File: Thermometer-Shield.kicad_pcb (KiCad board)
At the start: 2 copper layers, 31 parts, among them J1 CONN_01X04, J2 CONN_01X02, J3 CONN_01X02, J4 CONN_01X02, J5 CONN_01X02, SW1 SW_SPST, SW2 SW_SPST, SW3 SW_SPST, SW4 SW_SPST, U1 ULN2803A

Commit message: schematic nearly done. PCB started
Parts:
- removed R0: 330, Resistors_SMD:R_0805_HandSoldering
- added J11: ShiftOut, Pin_Headers:Pin_Header_Straight_1x02_Pitch2.54mm, F.Cu at (171.4, 61.0)
- added J6: Out-D, Connectors:AK300-2, F.Cu at (181.6, 92.7)
- added J7: Out-E, Connectors:AK300-2, F.Cu at (191.8, 92.7)
- added J8: Out-F, Connectors:AK300-2, F.Cu at (201.9, 92.7)
- added JP1: CONN_02X02, Pin_Headers:Pin_Header_Straight_2x02_Pitch2.54mm, F.Cu at (190.5, 61.0)
- added O-A2: out, Connectors:1pin, F.Cu at (151.8, 125.7)
- added O-B2: out, Connectors:1pin, F.Cu at (165.7, 156.2)
- added Q1: Q_PNP_BCE, TO_SOT_Packages_THT:TO-92_Inline_Narrow_Oval, F.Cu at (154.9, 111.8)
- added Q2: Q_PNP_BCE, TO_SOT_Packages_THT:TO-92_Inline_Narrow_Oval, F.Cu at (148.6, 111.8)
- added Q3: Q_PNP_BCE, TO_SOT_Packages_THT:TO-92_Inline_Narrow_Oval, F.Cu at (155.6, 117.5)
- added Q4: Q_PNP_BCE, TO_SOT_Packages_THT:TO-92_Inline_Narrow_Oval, F.Cu at (149.9, 117.5)
- added R19: R, Resistors_SMD:R_0805_HandSoldering, B.Cu at (166.4, 74.9)
- added R20: R, Resistors_SMD:R_0805_HandSoldering, B.Cu at (172.1, 74.9)
- added R21: R, Resistors_SMD:R_0805_HandSoldering, B.Cu at (177.8, 74.3)
- added R22: R, Resistors_SMD:R_0805_HandSoldering, B.Cu at (184.2, 73.7)
- added U2: 74HC595, Housings_SSOP:TSSOP-16_4.4x5mm_Pitch0.65mm, B.Cu at (165.7, 62.9)
- added U3: ULN2803A, Housings_SOIC:SOIC-18W_7.5x11.6mm_Pitch1.27mm, B.Cu at (188.0, 81.3)
- J1: value CONN_01X04 -> Analog/I2C; footprint Pin_Headers:Pin_Header_Straight_1x04_Pitch2.54mm -> Pin_Headers:Pin_Header_Straight_1x06_Pitch2.54mm
- J2: value CONN_01X02 -> TempSensor; footprint Connectors:AK300-2 -> Pin_Headers:Pin_Header_Straight_1x04_Pitch2.54mm
- J3: value CONN_01X02 -> Out-A
- J4: value CONN_01X02 -> Out-B
- J5: value CONN_01X02 -> Out-C
- R1: value 330 -> A1050; footprint Resistors_SMD:R_0805_HandSoldering -> Opto-Devices:Resistor_LDR_D6.4_RM3.4; moved to F.Cu
- R10, R11, R12, R9: value 2K2 -> 330; footprint Resistors_SMD:R_0805_HandSoldering -> Resistors_SMD:R_0603_HandSoldering
- R15: value A1050 -> 2K2; footprint Opto-Devices:Resistor_LDR_D6.4_RM3.4 -> Resistors_SMD:R_0805_HandSoldering; moved to B.Cu
- R16, R17, R2: value 330 -> 2K2
- R3, R4, R5, R6, R7, R8: footprint Resistors_SMD:R_0805_HandSoldering -> Resistors_SMD:R_0603_HandSoldering
- U1: value ULN2803A -> 74HC595; footprint Housings_SOIC:SOIC-18W_7.5x11.6mm_Pitch1.27mm -> Housings_SSOP:TSSOP-16_4.4x5mm_Pitch0.65mm
- moved J1 107.9 mm to (222.9, 80.0), turned to 0 degrees
- moved R2 72.5 mm to (198.1, 100.3), turned to 180 degrees
- moved R4 65.3 mm to (144.8, 85.7)
- moved R1 64.8 mm to (212.1, 85.1)
- moved R5 60.5 mm to (144.8, 82.5)
- moved R12 60.4 mm to (144.8, 60.3), turned to 0 degrees
- moved R6 56.1 mm to (144.8, 79.4)
- moved R11 55.7 mm to (144.8, 63.5), turned to 0 degrees
- moved J2 52.2 mm to (201.3, 74.3), turned to 90 degrees
- moved Disp1 52.0 mm to (123.8, 64.1)
- moved R7 52.0 mm to (144.8, 76.2)
- moved R8 48.5 mm to (144.8, 73.0)
- moved R3 47.8 mm to (144.8, 54.6)
- moved R17 45.6 mm to (217.8, 109.2)
- moved R10 45.1 mm to (144.8, 66.7), turned to 0 degrees
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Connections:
- Disp1 pad 10: Net-(Disp1-Pad10) -> Dig2
- Disp1 pad 11: F -> Net-(Disp1-Pad11)
- Disp1 pad 13: C -> Net-(Disp1-Pad13)
- Disp1 pad 14: A -> Net-(Disp1-Pad14)
- Disp1 pad 15: G -> Net-(Disp1-Pad15)
- Disp1 pad 16: B -> Net-(Disp1-Pad16)
- Disp1 pad 3: D -> Net-(Disp1-Pad3)
- Disp1 pad 4: Extras -> Dig1
- Disp1 pad 5: E -> Net-(Disp1-Pad5)
- Disp1 pad 7: DP -> Net-(Disp1-Pad7)
- Disp1 pad 9: Extras -> Net-(Disp1-Pad9)
- J1 pad 1: +5V -> GND
- J1 pad 2: Temp-Data -> +5V
- J1 pad 3: (no net) -> Net-(J1-Pad3)
- J1 pad 4: GND -> Net-(J1-Pad4)
- J2 pad 1: /Out-A -> +5V
- J2 pad 2: GND -> Temp-Data
- J3 pad 1: /Out-B -> /Out-A
- J3 pad 2: GND -> VCC
- J4 pad 1: /Out-C -> /Out-B
- J4 pad 2: GND -> VCC
- J5 pad 1: /Out-D -> /Out-C
- J5 pad 2: GND -> VCC
- R1 pad 1: DP -> +5V
- R1 pad 2: Net-(R1-Pad2) -> Light
- R10 pad 1: Net-(R10-Pad1) -> Net-(Disp1-Pad7)
- R10 pad 2: Net-(R10-Pad2) -> DP
- R11 pad 1: Net-(R10-Pad2) -> Colon
- R11 pad 2: Net-(R11-Pad2) -> Net-(Disp1-Pad9)
- R12 pad 1: Net-(R11-Pad2) -> Degree
- R12 pad 2: Net-(R12-Pad2) -> Net-(Disp1-Pad12)
- R13 pad 1: Net-(R12-Pad2) -> +5V
- R13 pad 2: Buttons -> Net-(R13-Pad2)
- R14 pad 1: Buttons -> Net-(R13-Pad2)
- R14 pad 2: GND -> Net-(R14-Pad2)
- R15 pad 1: +5V -> Net-(R14-Pad2)
- R15 pad 2: Light -> Net-(R15-Pad2)
- R16 pad 1: Net-(Disp1-Pad10) -> Net-(R15-Pad2)
- R16 pad 2: +5V -> Net-(R16-Pad2)
- R17 pad 1: Net-(Disp1-Pad12) -> Net-(R16-Pad2)
- R17 pad 2: GND -> Buttons
- R18 pad 1: Light -> Buttons
- R2 pad 1: C -> Light
- R2 pad 2: Net-(R2-Pad2) -> GND
- R3 pad 1: B -> Net-(Disp1-Pad14)
- R3 pad 2: Net-(R3-Pad2) -> A
- R4 pad 1: A -> Net-(Disp1-Pad16)
- R4 pad 2: Net-(R4-Pad2) -> B
- R5 pad 1: F -> Net-(Disp1-Pad13)
- R5 pad 2: Net-(R5-Pad2) -> C
- R6 pad 1: G -> Net-(Disp1-Pad3)
- R6 pad 2: Net-(R6-Pad2) -> D
- R7 pad 1: D -> Net-(Disp1-Pad5)
- R7 pad 2: Net-(R7-Pad2) -> E
- R8 pad 1: E -> Net-(Disp1-Pad11)
- R8 pad 2: Net-(R8-Pad2) -> F
- R9 pad 1: +5V -> Net-(Disp1-Pad15)
- R9 pad 2: Net-(R10-Pad1) -> G
- SHIELD1 pad 0: Net-(R0-Pad2) -> (no net)
- SHIELD1 pad 1: Net-(R1-Pad2) -> (no net)
- SHIELD1 pad 10: Dig2 -> SS
- SHIELD1 pad 11: Dig3 -> MOSI
- SHIELD1 pad 12: Dig4 -> Net-(JP1-Pad1)
- SHIELD1 pad 13: Temp-Data -> SCK
- SHIELD1 pad 2: Net-(R2-Pad2) -> Temp-Data
- SHIELD1 pad 3: Net-(R3-Pad2) -> Trig-F
- SHIELD1 pad 4: Net-(R4-Pad2) -> Trig-E
- SHIELD1 pad 5: Net-(R5-Pad2) -> Trig-D
- SHIELD1 pad 6: Net-(R6-Pad2) -> Trig-C
- SHIELD1 pad 7: Net-(R7-Pad2) -> Trig-B
- SHIELD1 pad 8: Net-(R8-Pad2) -> Trig-A
- SHIELD1 pad 9: Dig1 -> Net-(JP1-Pad3)
- SHIELD1 pad AD2: Trig-D -> Net-(J1-Pad6)
- SHIELD1 pad AD3: Trig-C -> Net-(J1-Pad5)
- SHIELD1 pad AD4: Trig-B -> Net-(J1-Pad3)
- SHIELD1 pad AD5: Trig-A -> Net-(J1-Pad4)
- SHIELD1 pad V_IN: (no net) -> VCC
- SW1 pad 2: Net-(R10-Pad1) -> Net-(R13-Pad2)
- SW2 pad 2: Net-(R10-Pad2) -> Net-(R14-Pad2)
- SW3 pad 2: Net-(R11-Pad2) -> Net-(R15-Pad2)
- SW4 pad 2: Net-(R12-Pad2) -> Net-(R16-Pad2)
- U1 pad 1: Trig-A -> D
- U1 pad 11: /Out-D -> SCK
- U1 pad 12: /Out-D -> SS
- U1 pad 13: /Out-C -> GND
- U1 pad 14: /Out-C -> MOSI
- U1 pad 15: /Out-B -> E
- U1 pad 16: /Out-B -> VCC
- U1 pad 2: Trig-A -> G
- U1 pad 3: Trig-B -> F
- U1 pad 4: Trig-B -> A
- U1 pad 5: Trig-C -> B
- U1 pad 6: Trig-C -> C
- U1 pad 7: Trig-D -> DP
- U1 pad 8: Trig-D -> GND
- U1 pad 9: GND -> Net-(U1-Pad9)
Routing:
- net +5V: track 96.9 -> 0.00 mm
- net Trig-D: track 65.1 -> 0.00 mm
- net /Out-D: track 23.9 -> 0.00 mm
- net /Out-C: track 16.6 -> 0.00 mm
- net GND: track 16.5 -> 0.00 mm
- net Net-(R10-Pad2): track 15.9 -> 0.00 mm
- net Net-(R10-Pad1): track 15.8 -> 0.00 mm
- net Net-(R11-Pad2): track 10.8 -> 0.00 mm
- net Light: track 10.3 -> 0.00 mm
- net /Out-A: track 10.0 -> 0.00 mm
- net Net-(R12-Pad2): track 9.53 -> 0.00 mm
- net /Out-B: track 7.93 -> 0.00 mm
- net Buttons: track 7.79 -> 0.00 mm
- net Trig-A: track 2.29 -> 0.00 mm
- net Trig-C: track 1.27 -> 0.00 mm
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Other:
- net class Output removed
- net class Output-Gnd removed

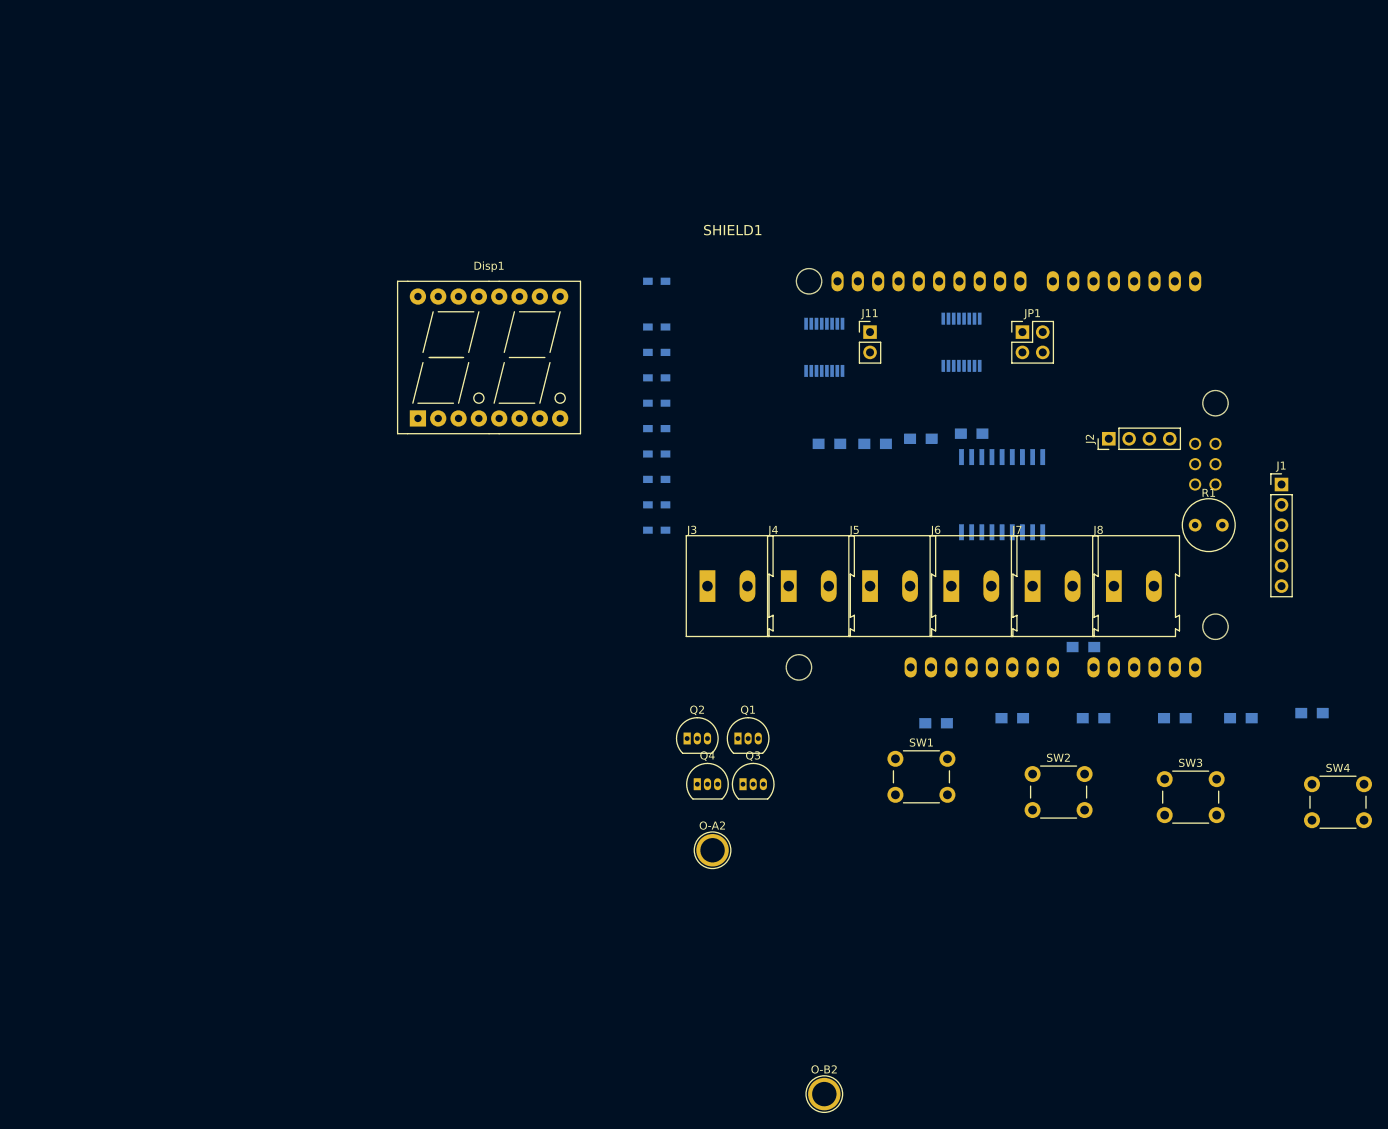
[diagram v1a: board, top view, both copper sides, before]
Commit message: completed schematic and pcb
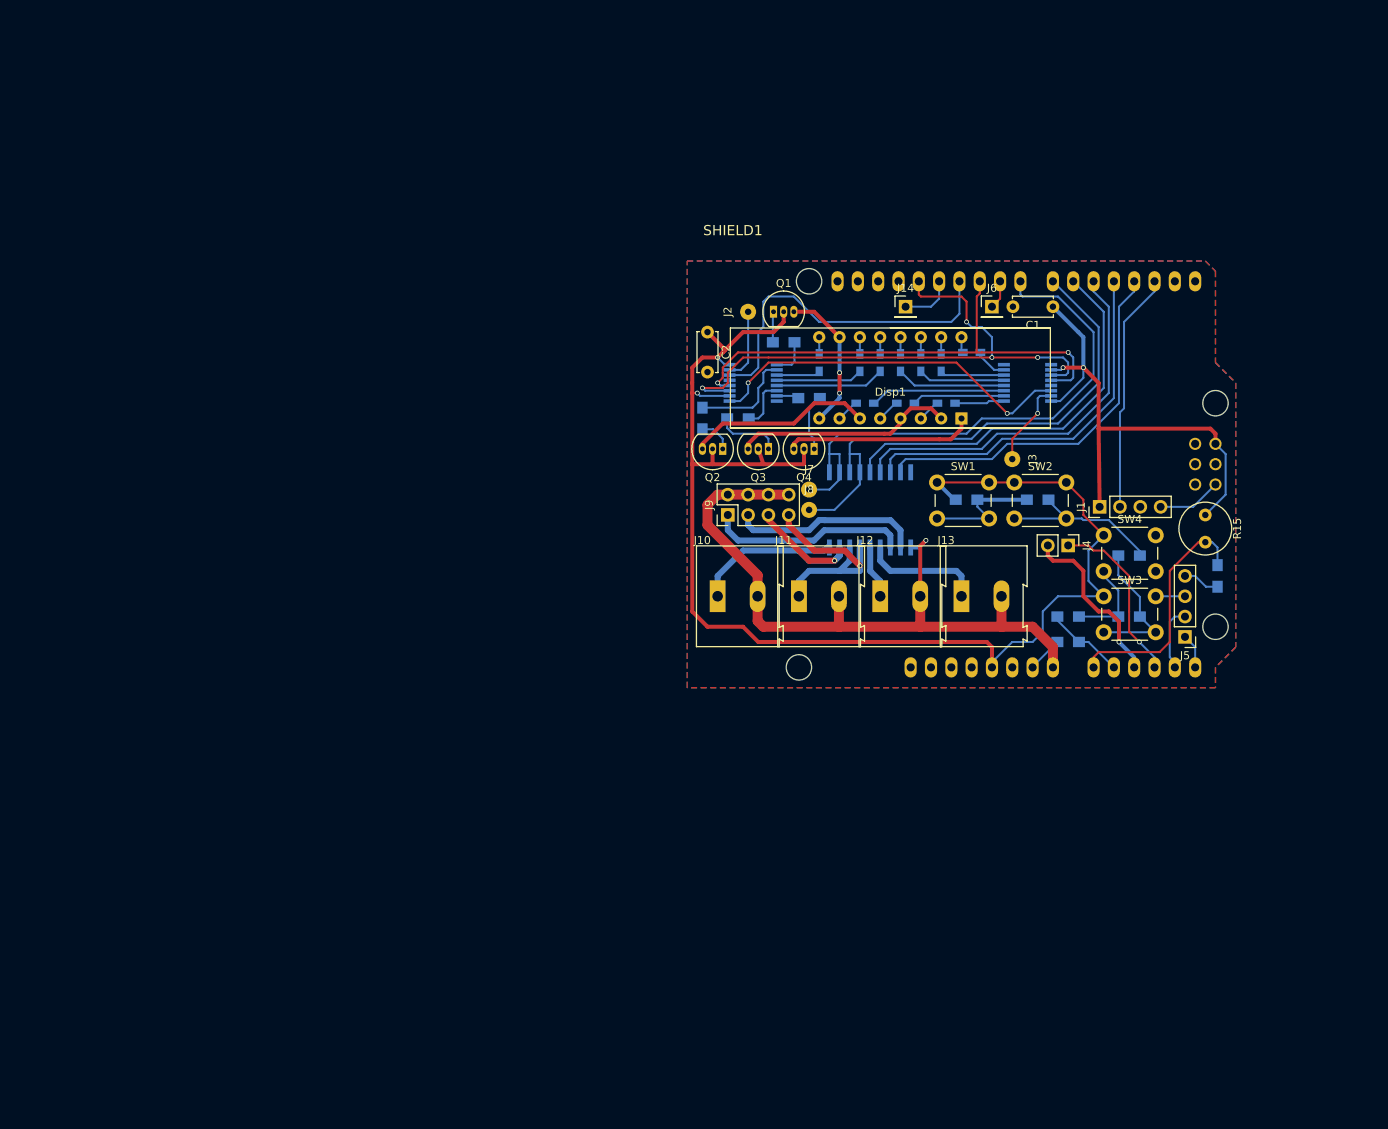
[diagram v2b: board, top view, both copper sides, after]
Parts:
- removed JP1: CONN_02X02, Pin_Headers:Pin_Header_Straight_2x02_Pitch2.54mm
- removed O-A2, O-B2: out, Connectors:1pin
- added C1: C, Capacitors_THT:C_Disc_D5.0mm_W2.5mm_P5.00mm, F.Cu at (194.3, 57.8)
- added C2: C, Capacitors_THT:C_Disc_D5.0mm_W2.5mm_P5.00mm, F.Cu at (151.1, 61.0)
- added J10: Out-A, Connectors:AK300-2, F.Cu at (152.4, 94.0)
- added J12: Out-C, Connectors:AK300-2, F.Cu at (172.7, 94.0)
- added J13: Out-D, Connectors:AK300-2, F.Cu at (182.9, 94.0)
- added J14: Pin12, Pin_Headers:Pin_Header_Straight_1x01_Pitch2.54mm, F.Cu at (175.9, 57.8)
- added J9: Outputs, Pin_Headers:Pin_Header_Straight_2x04_Pitch2.54mm, F.Cu at (153.7, 83.8)
- Disp1: footprint Displays_7-Segment:AFF_2x7SEG-DIGIT_10mm -> SparkFun:ATA3492
- J1: value Analog/I2C -> TempSensor; footprint Pin_Headers:Pin_Header_Straight_1x06_Pitch2.54mm -> Pin_Headers:Pin_Header_Straight_1x04_Pitch2.54mm
- J11: value ShiftOut -> Out-B; footprint Pin_Headers:Pin_Header_Straight_1x02_Pitch2.54mm -> Connectors:AK300-2
- J2: value TempSensor -> Shift-A; footprint Pin_Headers:Pin_Header_Straight_1x04_Pitch2.54mm -> Wire_Pads:SolderWirePad_single_0-8mmDrill
- J3: value Out-A -> Shift-B; footprint Connectors:AK300-2 -> Wire_Pads:SolderWirePad_single_0-8mmDrill
- J4: value Out-B -> Analog; footprint Connectors:AK300-2 -> Pin_Headers:Pin_Header_Straight_1x02_Pitch2.54mm
- J5: value Out-C -> I2C; footprint Connectors:AK300-2 -> Pin_Headers:Pin_Header_Straight_1x04_Pitch2.54mm
- J6: value Out-D -> Pin9; footprint Connectors:AK300-2 -> Pin_Headers:Pin_Header_Straight_1x01_Pitch2.54mm
- J7: value Out-E -> Trig-G; footprint Connectors:AK300-2 -> Wire_Pads:SolderWirePad_single_0-8mmDrill
- J8: value Out-F -> Trig-H; footprint Connectors:AK300-2 -> Wire_Pads:SolderWirePad_single_0-8mmDrill
- R1: value A1050 -> R; footprint Opto-Devices:Resistor_LDR_D6.4_RM3.4 -> Resistors_SMD:R_0805_HandSoldering; moved to B.Cu
- R13, R14: value 2K2 -> 330; footprint Resistors_SMD:R_0805_HandSoldering -> Resistors_SMD:R_0603_HandSoldering
- R15: value 2K2 -> A1050; footprint Resistors_SMD:R_0805_HandSoldering -> Opto-Devices:Resistor_LDR_D6.4_RM3.4; moved to F.Cu
- R19, R20, R21, R22: value R -> 2K2
- R2: value 2K2 -> R
- R3, R4: value 330 -> R; footprint Resistors_SMD:R_0603_HandSoldering -> Resistors_SMD:R_0805_HandSoldering
- moved R1 56.3 mm to (160.7, 62.2)
- moved R2 55.5 mm to (150.5, 71.8), turned to 90 degrees
- moved Q1 53.5 mm to (159.4, 58.4)
- moved Disp1 50.2 mm to (174.0, 66.7)
- moved J2 47.8 mm to (156.2, 58.4)
- moved R14 47.4 mm to (172.7, 64.8), turned to 90 degrees
- moved R13 47.4 mm to (165.1, 64.8), turned to 90 degrees
- moved Q4 44.4 mm to (164.5, 75.6), turned to 180 degrees
- moved R17 43.8 mm to (183.5, 81.9)
- moved R18 43.4 mm to (192.4, 81.9)
- moved R6 42.5 mm to (184.2, 63.5)
- moved Q3 42.0 mm to (158.8, 75.6), turned to 180 degrees
- moved J3 41.3 mm to (189.2, 76.8), turned to 270 degrees
- moved SW4 40.6 mm to (200.7, 86.4)
- moved R19 40.0 mm to (203.8, 88.9), turned to 180 degrees
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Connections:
- Disp1 pad 10: Dig2 -> Dig1
- Disp1 pad 4: Dig1 -> Dig3
- J1 pad 1: GND -> VCC
- J1 pad 2: +5V -> Temp-Data
- J1 pad 3: Net-(J1-Pad3) -> (no net)
- J1 pad 4: Net-(J1-Pad4) -> GND
- J11 pad 1: Net-(J11-Pad1) -> /Out-B
- J11 pad 2: Net-(J11-Pad2) -> VSS
- J2 pad 1: +5V -> Net-(J2-Pad1)
- J3 pad 1: /Out-A -> Net-(J3-Pad1)
- J4 pad 1: /Out-B -> Net-(J4-Pad1)
- J4 pad 2: VCC -> Net-(J4-Pad2)
- J5 pad 1: /Out-C -> Net-(J5-Pad1)
- J5 pad 2: VCC -> Net-(J5-Pad2)
- J6 pad 1: /Out-D -> Net-(J6-Pad1)
- J7 pad 1: /Out-E -> Trig-A
- J8 pad 1: /Out-F -> Trig-B
- Q1 pad 2: +5V -> VCC
- Q2 pad 2: +5V -> VCC
- Q3 pad 2: +5V -> VCC
- Q4 pad 2: +5V -> VCC
- R1 pad 1: +5V -> Net-(Q1-Pad1)
- R1 pad 2: Light -> Dig1_En
- R10 pad 1: Net-(Disp1-Pad7) -> Net-(Disp1-Pad11)
- R10 pad 2: DP -> F
- R11 pad 1: Colon -> Net-(Disp1-Pad15)
- R11 pad 2: Net-(Disp1-Pad9) -> G
- R12 pad 1: Degree -> Net-(Disp1-Pad7)
- R12 pad 2: Net-(Disp1-Pad12) -> DP
- R13 pad 1: +5V -> Colon
- R13 pad 2: Net-(R13-Pad2) -> Net-(Disp1-Pad9)
- R14 pad 1: Net-(R13-Pad2) -> Degree
- R14 pad 2: Net-(R14-Pad2) -> Net-(Disp1-Pad12)
- R15 pad 1: Net-(R14-Pad2) -> VCC
- R15 pad 2: Net-(R15-Pad2) -> Light
- R16 pad 1: Net-(R15-Pad2) -> Light
- R16 pad 2: Net-(R16-Pad2) -> GND
- R17 pad 1: Net-(R16-Pad2) -> VCC
- R17 pad 2: Buttons -> Net-(R17-Pad2)
- R18 pad 1: Buttons -> Net-(R17-Pad2)
- R18 pad 2: GND -> Net-(R18-Pad2)
- R19 pad 1: Net-(Q1-Pad1) -> Net-(R18-Pad2)
- R19 pad 2: Dig1_En -> Net-(R19-Pad2)
- R2 pad 1: Light -> Net-(Q2-Pad1)
- R2 pad 2: GND -> Dig2_En
- R20 pad 1: Net-(Q2-Pad1) -> Net-(R19-Pad2)
- R20 pad 2: Dig2_En -> Net-(R20-Pad2)
- R21 pad 1: Net-(Q3-Pad1) -> Net-(R20-Pad2)
- R21 pad 2: Dig3_En -> Buttons
- R22 pad 1: Net-(Q4-Pad1) -> Buttons
- R22 pad 2: Dig4_En -> GND
- R3 pad 1: Net-(Disp1-Pad14) -> Net-(Q3-Pad1)
- R3 pad 2: A -> Dig3_En
- R4 pad 1: Net-(Disp1-Pad16) -> Net-(Q4-Pad1)
- R4 pad 2: B -> Dig4_En
- R5 pad 1: Net-(Disp1-Pad13) -> Net-(Disp1-Pad14)
- R5 pad 2: C -> A
- R6 pad 1: Net-(Disp1-Pad3) -> Net-(Disp1-Pad16)
- R6 pad 2: D -> B
- R7 pad 1: Net-(Disp1-Pad5) -> Net-(Disp1-Pad13)
- R7 pad 2: E -> C
- R8 pad 1: Net-(Disp1-Pad11) -> Net-(Disp1-Pad3)
- R8 pad 2: F -> D
- R9 pad 1: Net-(Disp1-Pad15) -> Net-(Disp1-Pad5)
- R9 pad 2: G -> E
- SHIELD1 pad 5V: +5V -> VCC
- SHIELD1 pad 9: Net-(JP1-Pad3) -> Net-(J6-Pad1)
- SHIELD1 pad AD2: Net-(J1-Pad6) -> Net-(J4-Pad2)
- SHIELD1 pad AD3: Net-(J1-Pad5) -> Net-(J4-Pad1)
- SHIELD1 pad AD4: Net-(J1-Pad3) -> Net-(J5-Pad2)
- SHIELD1 pad AD5: Net-(J1-Pad4) -> Net-(J5-Pad1)
- SHIELD1 pad SP2: (no net) -> VCC
- SHIELD1 pad SP6: (no net) -> GND
- SHIELD1 pad V_IN: VCC -> VSS
- SW1 pad 1: +5V -> VCC
- SW1 pad 2: Net-(R13-Pad2) -> Net-(R17-Pad2)
- SW2 pad 1: +5V -> VCC
- SW2 pad 2: Net-(R14-Pad2) -> Net-(R18-Pad2)
- SW3 pad 1: +5V -> VCC
- SW3 pad 2: Net-(R15-Pad2) -> Net-(R19-Pad2)
- SW4 pad 1: +5V -> VCC
- SW4 pad 2: Net-(R16-Pad2) -> Net-(R20-Pad2)
- U1 pad 1: D -> Dig1_En
- U1 pad 10: +5V -> VCC
- U1 pad 15: E -> Net-(J2-Pad1)
- U1 pad 2: G -> Dig2_En
- U1 pad 3: F -> Colon
- U1 pad 4: A -> F
- U1 pad 5: B -> Degree
- U1 pad 6: C -> Dig3_En
- U1 pad 7: DP -> Dig4_En
- U2 pad 1: Net-(J11-Pad2) -> D
- U2 pad 10: +5V -> VCC
- U2 pad 15: Net-(J11-Pad1) -> Net-(J3-Pad1)
- U2 pad 2: Dig4_En -> E
- U2 pad 3: Dig3_En -> DP
- U2 pad 4: Dig2_En -> C
- U2 pad 5: Dig1_En -> A
- U2 pad 6: Colon -> G
- U2 pad 7: Degree -> B
- U3 pad 10: VCC -> VSS
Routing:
- net VCC: track 0.00 -> 242.5 mm, vias 0 -> 4
- net VSS: track 0.00 -> 89.8 mm, vias 0 -> 1
- net SCK: track 0.00 -> 72.7 mm, vias 0 -> 4
- net Trig-A: track 0.00 -> 67.2 mm
- net Trig-B: track 0.00 -> 65.6 mm
- net SS: track 0.00 -> 63.9 mm, vias 0 -> 2
- net Trig-C: track 0.00 -> 49.5 mm
- net Trig-D: track 0.00 -> 48.4 mm
- net Trig-F: track 0.00 -> 47.5 mm
- net Trig-E: track 0.00 -> 47.4 mm
- net Net-(U1-Pad9): track 0.00 -> 46.7 mm, vias 0 -> 2
- net MOSI: track 0.00 -> 43.1 mm
- net /Out-A: track 0.00 -> 37.8 mm, vias 0 -> 1
- net /Out-B: track 0.00 -> 31.0 mm, vias 0 -> 1
- net Light: track 0.00 -> 30.4 mm
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- added copper zone on B.Cu, net GND
- added copper zone on F.Cu, net GND
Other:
- net class Dig-Anode added: clearance 0.2, trace_width 0.5, via_dia 0.6, via_drill 0.4
- net class Output added: clearance 0.5, trace_width 0.75, via_dia 0.6, via_drill 0.4
